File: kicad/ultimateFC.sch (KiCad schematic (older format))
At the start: 196 parts, among them J1 USB_B_Micro, J2 10132797-011100LF, J3 10132797-011100LF, J4 10132797-011100LF, J5 10132797-011100LF, J6 10132797-011100LF, Q1 DMP2066LSN-7, U1 EFM8BB21F16G-C-QFN20R, U10 NCP81253MNTBG, U11 SiZ200DT, U12 NCP81253MNTBG, U13 SiZ200DT, U14 TPS62821, U15 SiZ200DT, U16 NCP81253MNTBG, U17 NCP81253MNTBG, U18 NCP81253MNTBG, U19 NCP81253MNTBG, U2 EFM8BB21F16G-C-QFN20R, U20 SiZ200DT, U21 SiZ200DT, U22 SiZ200DT, U23 SiZ200DT, U24 EFM8BB21F16G-C-QFN20R, U25 NCP81253MNTBG, U26 SiZ200DT, U27 NCP81253MNTBG, U28 NCP81253MNTBG, U29 SiZ200DT, U3 NCP81253MNTBG, U30 SiZ200DT, U31 INA186, U32 LMR33630CQRNX, U33 STM32F745VGHx, U34 AB7456, U35 ZOE-M8Q_ZOE-M8Q, U36 ICM-20602, U37 S25FL064L, U38 LIS3MDL, U39 BMP280, U4 SiZ200DT, U5 TPS630701, U6 EFM8BB21F16G-C-QFN20R, U7 NCP81253MNTBG, U8 SiZ200DT, U9 NCP81253MNTBG, X1 Molex_734120110, Y1 CSTNE8M00G550000R0, Y2 ECS-270-8-47Q-CES-TR

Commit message: changed motor pins for more TIMER/ DMA / ADC Support
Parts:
- removed C53: 2.2µF, Capacitor_SMD:C_0402_1005Metric, symbol Device:C
- removed U38: LIS3MDL, Package_LGA:LGA-12_2x2mm_P0.5mm, symbol own_devices:LIS3MDL
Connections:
- net labels added: (TIM1_CH1), (TIM1_CH2, UART2_RX, UART2_TX
- net labels removed: CS_BERGSTAK20, SPI1_NSS, UART1_RX, UART1_TX
- wire segments 889 -> 878
- no-connect marks 43 -> 41
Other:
- note added: "A02 - TIM2_CH3 - DMA1_S1_CH3 (ADC123_IN2)"
- note added: "A03 - TIM2_CH4 - DMA1_S6_CH3 (ADC123_IN3)"
- note added: "ADC 1\n"
- note added: "B00 - TIM3_CH4 - DMA1_S2_CH5 (ADC12_IN8)"
- note added: "B01 - TIM3_CH3 - DMA1_S7_CH5 (ADC12_IN9)"
- note added: "B06 - TIM4_CH1 - DMA1_S0_CH2"
- note added: "B07 - TIM4_CH2 - DMA1_S3_CH2"
- note added: "Bottom MP\nPins"
- note added: "DMA"
- note added: "DMA1 Stream 0"
- note added: "DMA1 Stream 1"
- note added: "DMA1 Stream 2"
- note added: "DMA1 Stream 3\n"
- note added: "DMA1 Stream 4"
- note added: "DMA1 Stream 5"
- note added: "DMA1 Stream 6"
- note added: "DMA1 Stream 7"
- note added: "DMA2 Stream 0"
- note added: "DMA2 Stream 1"
- note added: "DMA2 Stream 2"
- note added: "DMA2 Stream 3\n"
- note added: "DMA2 Stream 4"
- note added: "DMA2 Stream 5"
- note added: "DMA2 Stream 6"
- note added: "DMA2 Stream 7"
- note added: "E09 - TIM1_CH1 - DMA2_S3_CH6"
- note added: "E11 - TIM1_CH2 - DMA2_S2_CH6"
- note added: "E13 - TIM1_CH3 - DMA2_S6_CH6"
- note added: "E14 - TIM1_CH4 - DMA2_S4_CH6"
- note added: "MOTORS"
- note added: "SPI2_TX OSD"
- note added: "SPI4_TX Flash"
- note added: "TIM1_CH1\n"
- note added: "TIM1_CH2\n"
- note added: "TIM1_CH3"
- note added: "TIM1_CH4"
- note added: "TIM2_CH3"
- note added: "TIM2_CH4"
- note added: "TIM3_CH3"
- note added: "TIM3_CH4"
- note added: "TIM4_CH1"
- note added: "TIM4_CH2"
- note added: "The Capacitance change due to DC bias has to be considered \n(up to 4V on C47 und up to 2 V over C48 according to the simulation)\nTherefore changed to Tantals"
- note added: "Top MP\nPins"
- note added: "Valid Layerstack for BLD"
- note added: "Video connector\nMP Pins"
- note added: "WORKS ONLY WITH PROPER LAYER STACK AND LAYOUT!!"
- note added: "flash also usable for GPS - is there a convinient switching option?"
- note removed: "Bc und Bp getauscht\n"
- note removed: "FLash hinzufügen?"
- note removed: "MA und MB getauscht"
- note removed: "Pin assignments in parantheses (...) not checked in CubeMX!"
- note removed: "The Capacitance change due to DC bias has to be considered \n(up to 4V on C47 und up to 2 V over C48 according to the simulation)\nTherefore chnage to Tantals"
- moved on the sheet: C10, C17, C31, C32, C34, C47, C48, C49, C50, C51, C9, D2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

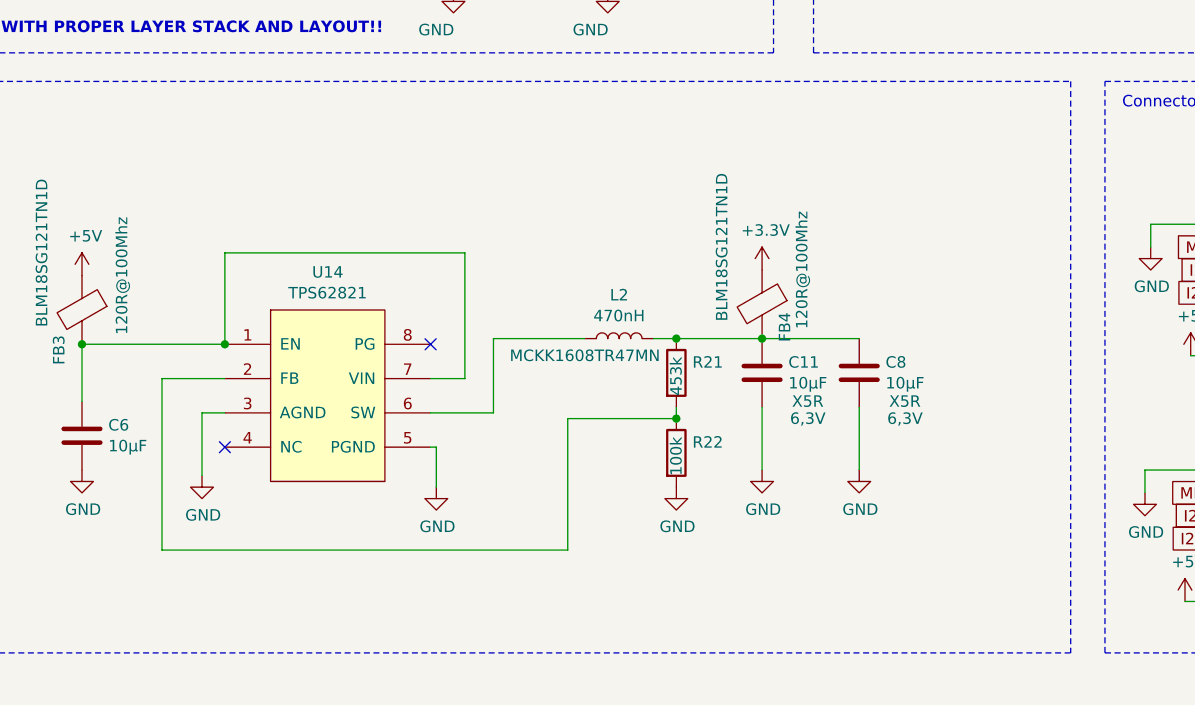
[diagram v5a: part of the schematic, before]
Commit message: changed 3.3V dcdc converter to one with forced pwm
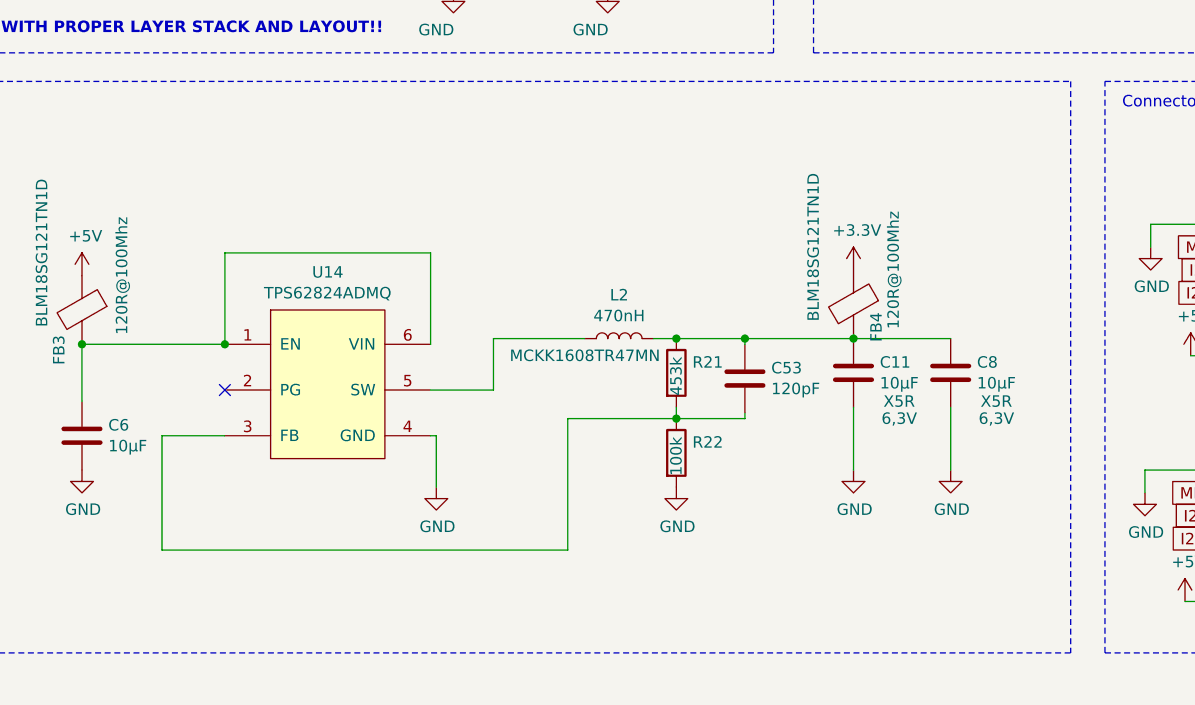
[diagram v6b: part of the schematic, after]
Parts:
- removed U14: TPS62821, ultimateFC:VSON-8HR, symbol lib_ultimateFC:TPS62821
- added C53: 120pF, Capacitor_SMD:C_0201_0603Metric, symbol Device:C
- added U14: TPS62824ADMQ, ultimateFC:VSON_HR6, symbol lib_ultimateFC:TPS62824ADMQ
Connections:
- net GND: now also U14.4 (GND)
- net at C6.1, FB3.2: now also U14.1 (EN), U14.6 (VIN)
- net at C11.1, C8.1, FB4.2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: now also C53.1
- net at R21.2, R22.1: now also C53.2, U14.3 (FB)
- net at L2.1: now also U14.5 (SW)
- no-connect marks 41 -> 40
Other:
- moved on the sheet: C11, C8, FB4
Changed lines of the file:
@@
 	14100 12050 14400 12050
 $Comp
-L lib_ultimateFC:TPS62821 U14
-U 1 1 5EF44ED0
-P 8475 14650
-F 0 "U14" H 8475 15165 50  0000 C CNN
-F 1 "TPS62821" H 8475 15074 50  0000 C CNN
-F 2 "ultimateFC:VSON-8HR" H 8275 14600 50  0001 C CNN
-F 3 "" H 8275 14600 50  0001 C CNN
-F 4 "1,01" H 8475 14650 50  0001 C CNN "price@100[€]"
-F 5 "0,734" H 8475 14650 50  0001 C CNN "price@10[€]"
-F 6 "0,478" H 8475 14650 50  0001 C CNN "price@1k[€]"
-	1    8475 14650
-	1    0    0    -1
-$EndComp
-$Comp
 L Device:C C11
 U 1 1 5EF8398C
-P 10375 14575
-F 0 "C11" H 10490 14621 50  0000 L CNN
-F 1 "10µF" H 10490 14530 50  0000 L CNN
-F 2 "Capacitor_SMD:C_0603_1608Metric" H 10413 14425 50  0001 C CNN
-F 3 "~" H 10375 14575 50  0001 C CNN
-F 4 "6,3V" H 10575 14375 50  0000 C CNN "Spannung"
-F 5 "X5R" H 10575 14450 50  0000 C CNN "Dielektrikum"
-F 6 "AMK107ABJ106KAHT" H 10375 14575 50  0001 C CNN "Mfr.No:"
-F 7 "0,053" H 10375 14575 50  0001 C CNN "price@100[€]"
-F 8 "0,149" H 10375 14575 50  0001 C CNN "price@10[€]"
-F 9 "0,041" H 10375 14575 50  0001 C CNN "price@1k[€]"
-	1    10375 14575
+P 10775 14575
+F 0 "C11" H 10890 14621 50  0000 L CNN
+F 1 "10µF" H 10890 14530 50  0000 L CNN
+F 2 "Capacitor_SMD:C_0603_1608Metric" H 10813 14425 50  0001 C CNN
+F 3 "~" H 10775 14575 50  0001 C CNN
+F 4 "6,3V" H 10975 14375 50  0000 C CNN "Spannung"
+F 5 "X5R" H 10975 14450 50  0000 C CNN "Dielektrikum"
+F 6 "AMK107ABJ106KAHT" H 10775 14575 50  0001 C CNN "Mfr.No:"
+F 7 "0,053" H 10775 14575 50  0001 C CNN "price@100[€]"
+F 8 "0,149" H 10775 14575 50  0001 C CNN "price@10[€]"
+F 9 "0,041" H 10775 14575 50  0001 C CNN "price@1k[€]"
+	1    10775 14575
 	1    0    0    -1
 $EndComp
@@
 $EndComp
 Wire Wire Line
-	8925 14600 9075 14600
-Wire Wire Line
-	9075 14600 9075 14050
-Wire Wire Line
-	9075 14050 8025 14050
-Wire Wire Line
 	8025 14050 8025 14450
 Wire Wire Line
 	7400 14450 7400 14700
-NoConn ~ 8025 14900
-NoConn ~ 8925 14450
+NoConn ~ 8025 14650
 $Comp
 L Device:L L2
@@
 L power:GND #PWR0255
 U 1 1 5F142120
-P 10375 15000
-F 0 "#PWR0255" H 10375 14750 50  0001 C CNN
-F 1 "GND" H 10380 14827 50  0000 C CNN
-F 2 "" H 10375 15000 50  0001 C CNN
-F 3 "" H 10375 15000 50  0001 C CNN
-	1    10375 15000
+P 10775 15000
+F 0 "#PWR0255" H 10775 14750 50  0001 C CNN
+F 1 "GND" H 10780 14827 50  0000 C CNN
+F 2 "" H 10775 15000 50  0001 C CNN
+F 3 "" H 10775 15000 50  0001 C CNN
+	1    10775 15000
 	1    0    0    -1
 $EndComp
@@
 	1    0    0    -1
 $EndComp
-$Comp
-L power:GND #PWR0257
-U 1 1 5F142B85
-P 7925 15025
-F 0 "#PWR0257" H 7925 14775 50  0001 C CNN
-F 1 "GND" H 7930 14852 50  0000 C CNN
-F 2 "" H 7925 15025 50  0001 C CNN
-F 3 "" H 7925 15025 50  0001 C CNN
-	1    7925 15025
-	1    0    0    -1
-$EndComp
 Wire Wire Line
 	7400 14450 8025 14450
-Connection ~ 8025 14450
-Wire Wire Line
-	8025 14750 7925 14750
-Wire Wire Line
-	7925 14750 7925 15025
-Wire Wire Line
-	8925 14900 8950 14900
-Wire Wire Line
-	8950 14900 8950 15075
 Wire Wire Line
-	9200 14425 9200 14750
-Wire Wire Line
-	9200 14750 8925 14750
-Wire Wire Line
-	10375 14725 10375 15000
+	10775 14725 10775 15000
 $Comp
 L Device:R R21
@@
 Connection ~ 10000 14425
 Wire Wire Line
-	10000 14425 10375 14425
+	10000 14425 10300 14425
 $Comp
 L Device:R R22
@@
 $EndComp
 Wire Wire Line
-	8025 14600 7750 14600
-Wire Wire Line
-	7750 14600 7750 15350
-Wire Wire Line
 	7750 15350 9525 15350
 Wire Wire Line
@@
 L power:+3.3V #PWR0260
 U 1 1 5F4695CF
-P 10375 14125
-F 0 "#PWR0260" H 10375 13975 50  0001 C CNN
-F 1 "+3.3V" H 10390 14298 50  0000 C CNN
-F 2 "" H 10375 14125 50  0001 C CNN
-F 3 "" H 10375 14125 50  0001 C CNN
-	1    10375 14125
+P 10775 14125
+F 0 "#PWR0260" H 10775 13975 50  0001 C CNN
+F 1 "+3.3V" H 10790 14298 50  0000 C CNN
+F 2 "" H 10775 14125 50  0001 C CNN
+F 3 "" H 10775 14125 50  0001 C CNN
+	1    10775 14125
 	1    0    0    -1
 $EndComp
@@
 L Device:Ferrite_Bead FB4
 U 1 1 5E733202
-P 10375 14275
-F 0 "FB4" V 10275 14175 50  0000 C CNN
-F 1 "120R@100Mhz" V 10200 14425 50  0000 C CNN
-F 2 "Inductor_SMD:L_0603_1608Metric" V 10305 14275 50  0001 C CNN
-F 3 "~" H 10375 14275 50  0001 C CNN
-F 4 "BLM18SG121TN1D" V 10550 14525 50  0000 C CNN "Mfr.No:"
-F 5 "0,064" H 10375 14275 50  0001 C CNN "price@100[€]"
-F 6 "0,043" H 10375 14275 50  0001 C CNN "price@10[€]"
-F 7 "0,039" H 10375 14275 50  0001 C CNN "price@1k[€]"
-	1    10375 14275
+P 10775 14275
+F 0 "FB4" V 10675 14175 50  0000 C CNN
+F 1 "120R@100Mhz" V 10600 14425 50  0000 C CNN
+F 2 "Inductor_SMD:L_0603_1608Metric" V 10705 14275 50  0001 C CNN
+F 3 "~" H 10775 14275 50  0001 C CNN
+F 4 "BLM18SG121TN1D" V 10950 14525 50  0000 C CNN "Mfr.No:"
+F 5 "0,064" H 10775 14275 50  0001 C CNN "price@100[€]"
+F 6 "0,043" H 10775 14275 50  0001 C CNN "price@10[€]"
+F 7 "0,039" H 10775 14275 50  0001 C CNN "price@1k[€]"
+	1    10775 14275
 	-1   0    0    -1
 $EndComp
-Connection ~ 10375 14425
+Connection ~ 10775 14425
 $Comp
 L Device:C C8
 U 1 1 5E735DD6
-P 10800 14575
-F 0 "C8" H 10915 14621 50  0000 L CNN
-F 1 "10µF" H 10915 14530 50  0000 L CNN
-F 2 "Capacitor_SMD:C_0603_1608Metric" H 10838 14425 50  0001 C CNN
-F 3 "~" H 10800 14575 50  0001 C CNN
-F 4 "6,3V" H 11000 14375 50  0000 C CNN "Spannung"
-F 5 "X5R" H 11000 14450 50  0000 C CNN "Dielektrikum"
-F 6 "AMK107ABJ106KAHT" H 10800 14575 50  0001 C CNN "Mfr.No:"
-F 7 "0,053" H 10800 14575 50  0001 C CNN "price@100[€]"
-F 8 "0,149" H 10800 14575 50  0001 C CNN "price@10[€]"
-F 9 "0,041" H 10800 14575 50  0001 C CNN "price@1k[€]"
-	1    10800 14575
+P 11200 14575
+F 0 "C8" H 11315 14621 50  0000 L CNN
+F 1 "10µF" H 11315 14530 50  0000 L CNN
+F 2 "Capacitor_SMD:C_0603_1608Metric" H 11238 14425 50  0001 C CNN
+F 3 "~" H 11200 14575 50  0001 C CNN
+F 4 "6,3V" H 11400 14375 50  0000 C CNN "Spannung"
+F 5 "X5R" H 11400 14450 50  0000 C CNN "Dielektrikum"
+F 6 "AMK107ABJ106KAHT" H 11200 14575 50  0001 C CNN "Mfr.No:"
+F 7 "0,053" H 11200 14575 50  0001 C CNN "price@100[€]"
+F 8 "0,149" H 11200 14575 50  0001 C CNN "price@10[€]"
+F 9 "0,041" H 11200 14575 50  0001 C CNN "price@1k[€]"
+	1    11200 14575
 	1    0    0    -1
 $EndComp
@@
 L power:GND #PWR0105
 U 1 1 5E73631C
-P 10800 15000
-F 0 "#PWR0105" H 10800 14750 50  0001 C CNN
-F 1 "GND" H 10805 14827 50  0000 C CNN
-F 2 "" H 10800 15000 50  0001 C CNN
-F 3 "" H 10800 15000 50  0001 C CNN
-	1    10800 15000
+P 11200 15000
+F 0 "#PWR0105" H 11200 14750 50  0001 C CNN
+F 1 "GND" H 11205 14827 50  0000 C CNN
+F 2 "" H 11200 15000 50  0001 C CNN
+F 3 "" H 11200 15000 50  0001 C CNN
+	1    11200 15000
 	1    0    0    -1
 $EndComp
 Wire Wire Line
-	10375 14425 10800 14425
+	10775 14425 11200 14425
 Wire Wire Line
-	10800 14725 10800 15000
+	11200 14725 11200 15000
 $Comp
 L lib_ultimateFC:EFM8BB10F8I-A-QFN20-MCU_SiliconLabs U2
@@
 Text Notes 28150 12050 0    50   ~ 10
 Valid Layerstack for BLD
+$Comp
+L lib_ultimateFC:TPS62824ADMQ U14
+U 1 1 609B39D9
+P 8475 14650
+F 0 "U14" H 8475 15165 50  0000 C CNN
+F 1 "TPS62824ADMQ" H 8475 15074 50  0000 C CNN
+F 2 "ultimateFC:VSON_HR6" H 8525 14650 50  0001 C CNN
+F 3 "" H 8525 14650 50  0001 C CNN
+	1    8475 14650
+	1    0    0    -1
+$EndComp
+Connection ~ 8025 14450
+Wire Wire Line
+	8925 14450 8925 14050
+Wire Wire Line
+	8925 14050 8025 14050
+Wire Wire Line
+	8925 14850 8950 14850
+Wire Wire Line
+	8950 14850 8950 15075
+Wire Wire Line
+	8025 14850 7750 14850
+Wire Wire Line
+	7750 14850 7750 15350
+Wire Wire Line
+	8925 14650 9200 14650
+Wire Wire Line
+	9200 14650 9200 14425
+$Comp
+L Device:C C53
+U 1 1 60DA7746
+P 10300 14600
+F 0 "C53" H 10415 14646 50  0000 L CNN
+F 1 "120pF" H 10415 14555 50  0000 L CNN
+F 2 "Capacitor_SMD:C_0201_0603Metric" H 10338 14450 50  0001 C CNN
+F 3 "~" H 10300 14600 50  0001 C CNN
+F 4 "NP0" H 10300 14600 50  0001 C CNN "Dielektrikum"
+F 5 "25V" H 10300 14600 50  0001 C CNN "Spannung"
+F 6 "" H 10300 14600 50  0001 C CNN "Mfr.No:"
+F 7 "" H 10300 14600 50  0001 C CNN "price@100[€]"
+F 8 "" H 10300 14600 50  0001 C CNN "price@10[€]"
+F 9 "" H 10300 14600 50  0001 C CNN "price@1k[€]"
+	1    10300 14600
+	1    0    0    -1
+$EndComp
+Wire Wire Line
+	10300 14450 10300 14425
+Connection ~ 10300 14425
+Wire Wire Line
+	10300 14425 10775 14425
+Wire Wire Line
+	10300 14750 10300 14775
+Wire Wire Line
+	10300 14775 10000 14775
 $EndSCHEMATC
